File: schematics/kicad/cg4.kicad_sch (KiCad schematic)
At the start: 0 parts

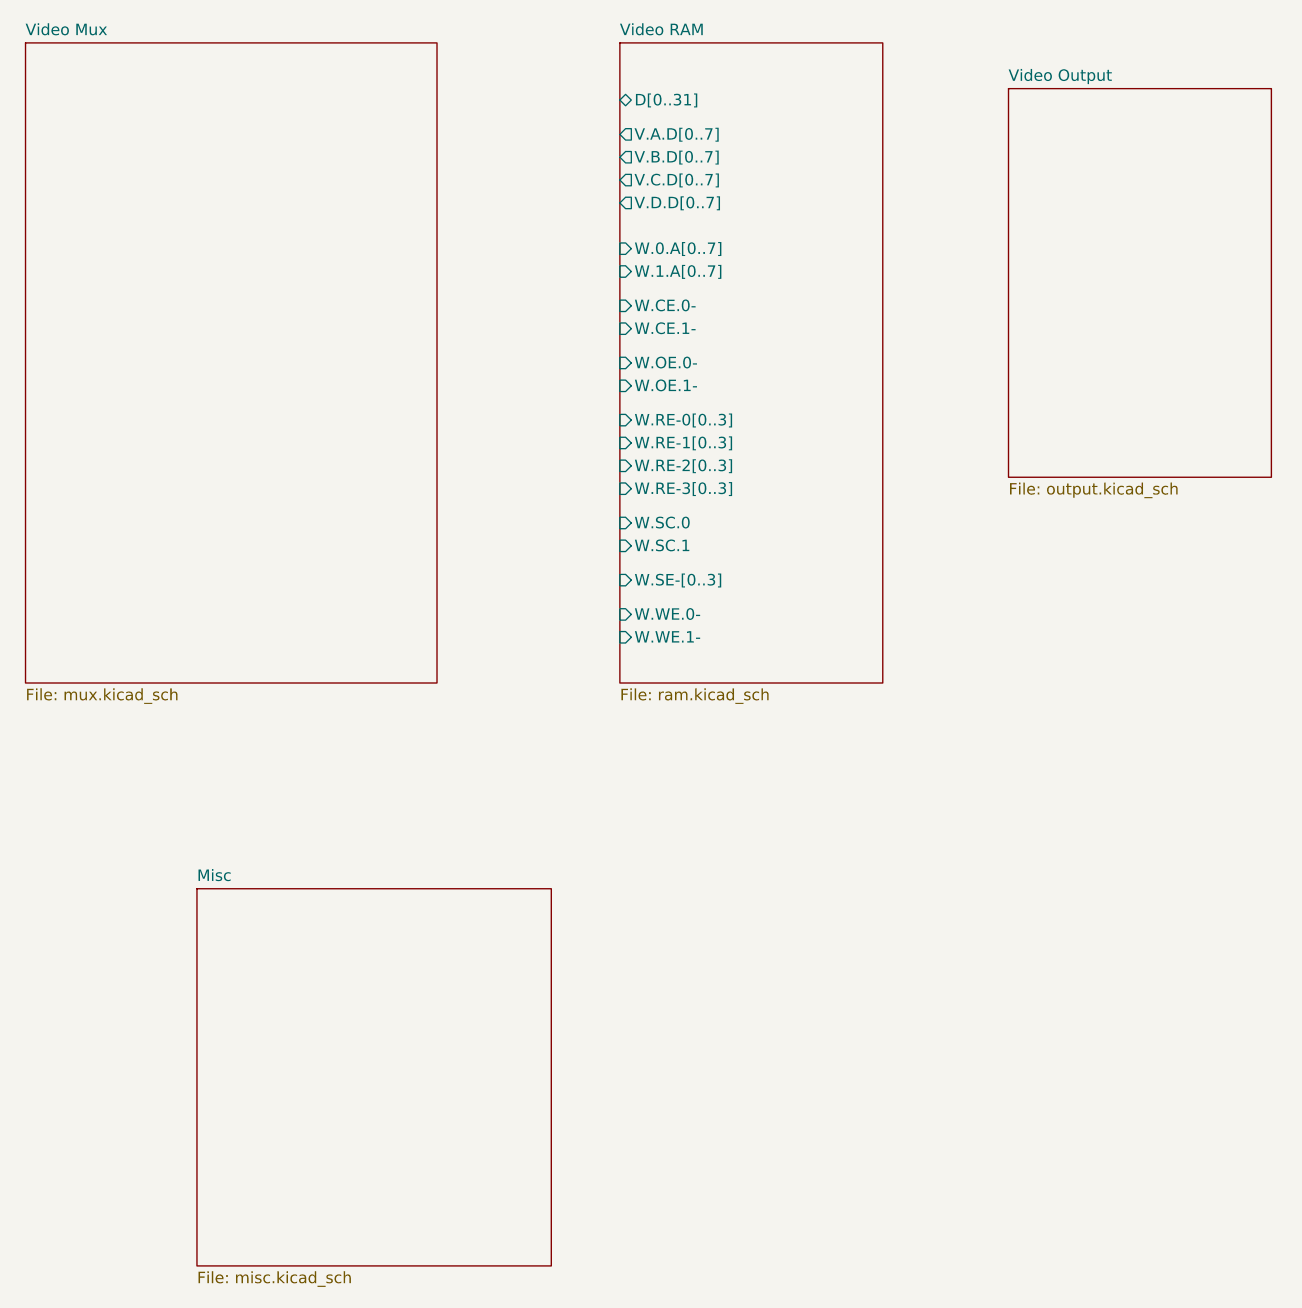
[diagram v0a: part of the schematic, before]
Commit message: Fill in more output section
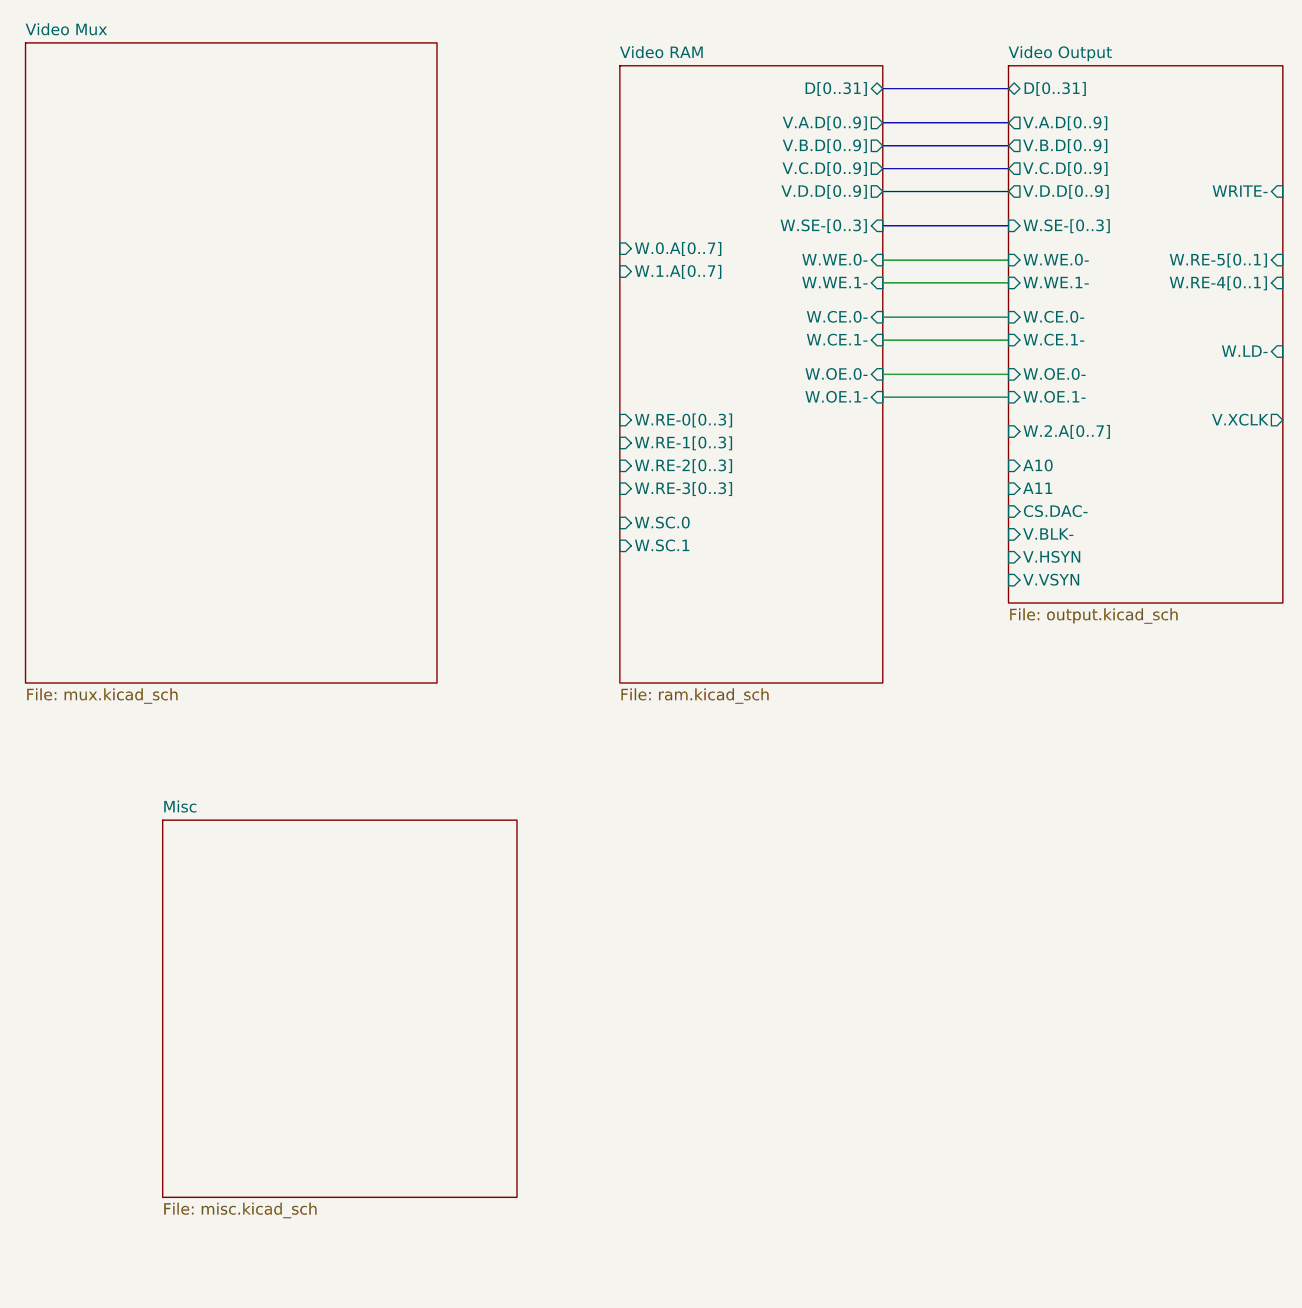
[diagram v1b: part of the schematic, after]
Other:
- sheet Video Output ports: added A10, A11, CS.DAC-, D[0..31], V.A.D[0..9], V.B.D[0..9], V.BLK-, V.C.D[0..9], V.D.D[0..9], V.HSYN, V.VSYN, V.XCLK, W.2.A[0..7], W.CE.0-, W.CE.1-, W.LD-, W.OE.0-, W.OE.1-, W.RE-4[0..1], W.RE-5[0..1], W.SE-[0..3], W.WE.0-, W.WE.1-, WRITE-; removed none
- sheet Video RAM ports: added V.A.D[0..9], V.B.D[0..9], V.C.D[0..9], V.D.D[0..9]; removed V.A.D[0..7], V.B.D[0..7], V.C.D[0..7], V.D.D[0..7]

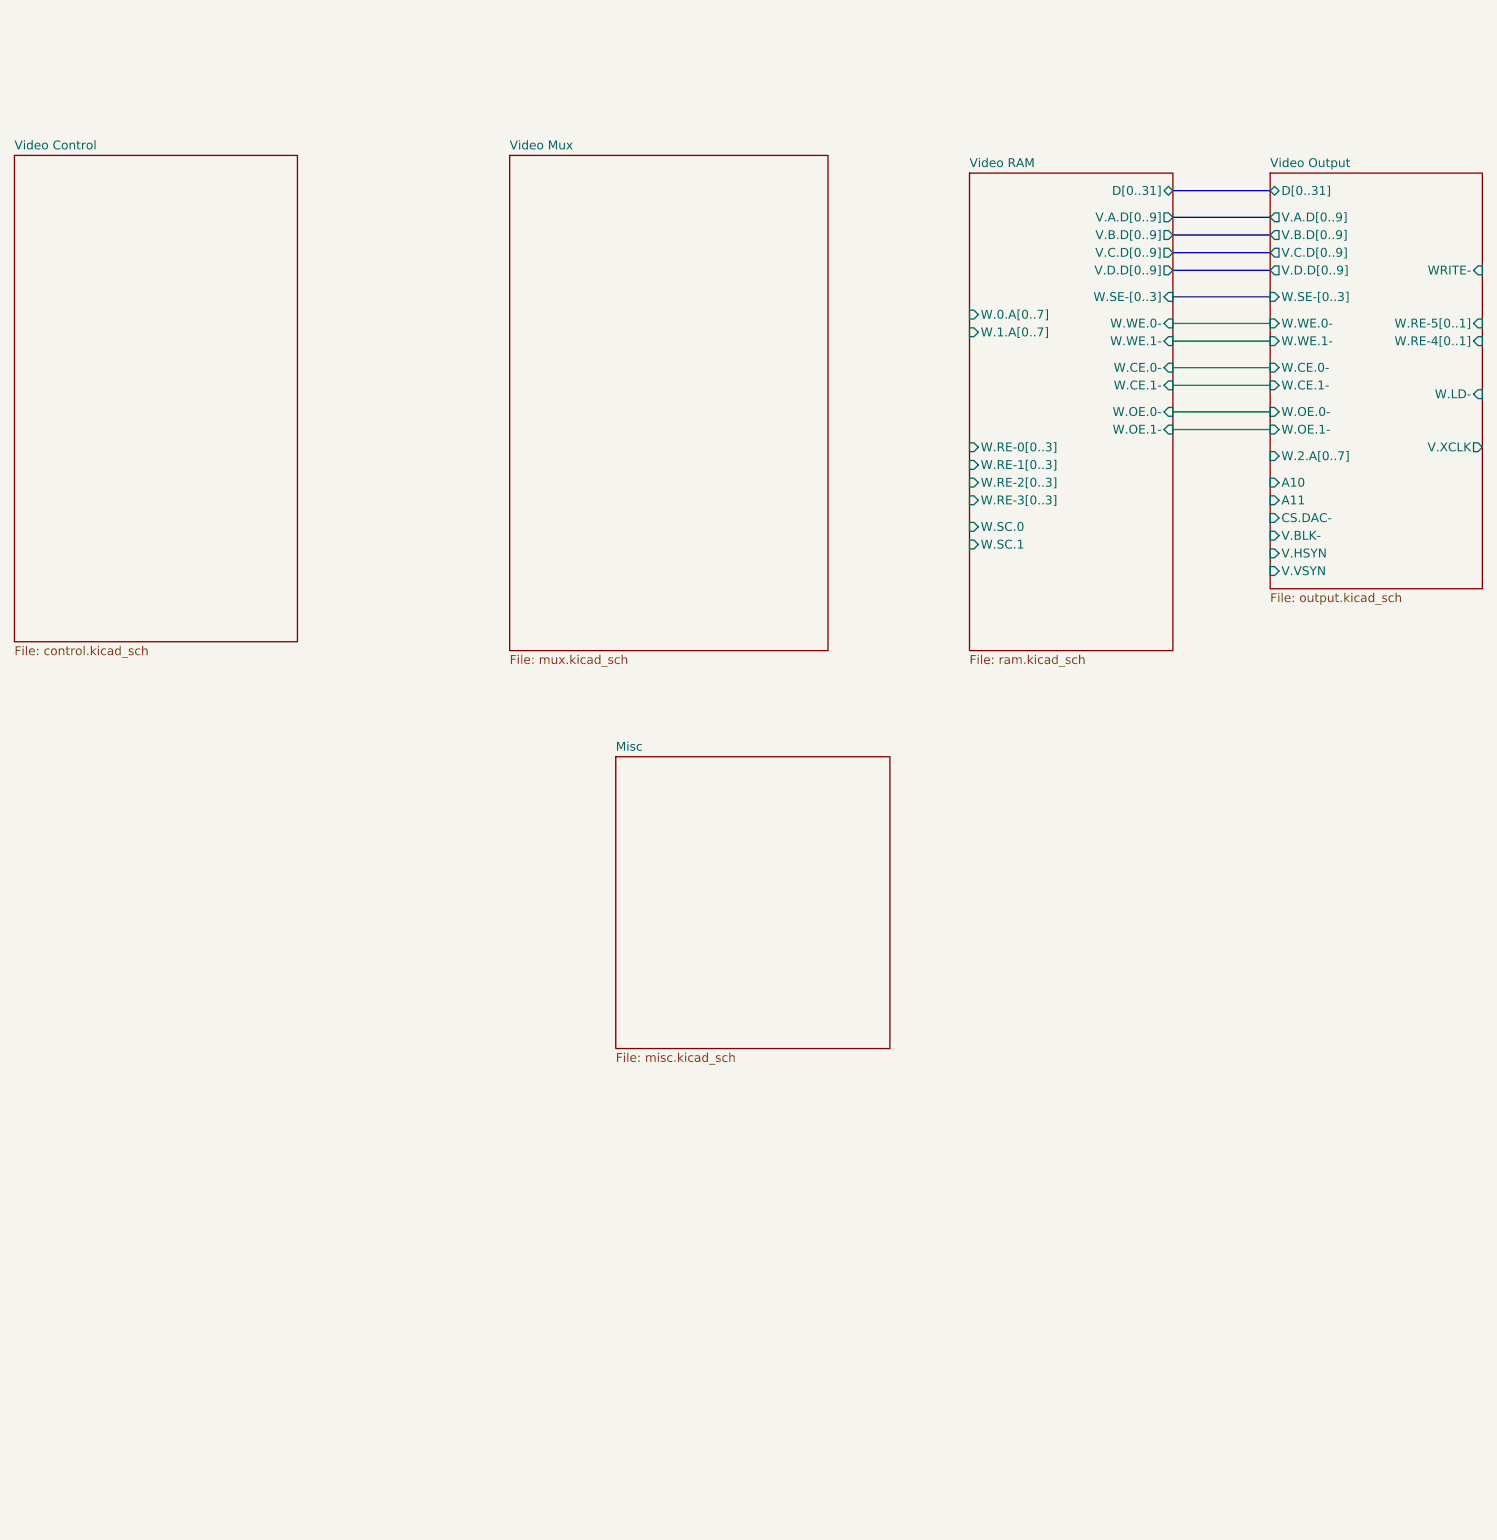
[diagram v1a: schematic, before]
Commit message: Populate misc page with P4 connector and caps Finish MUX, RAM and most of Output Lots of progress on Control Lay out root and connect most components
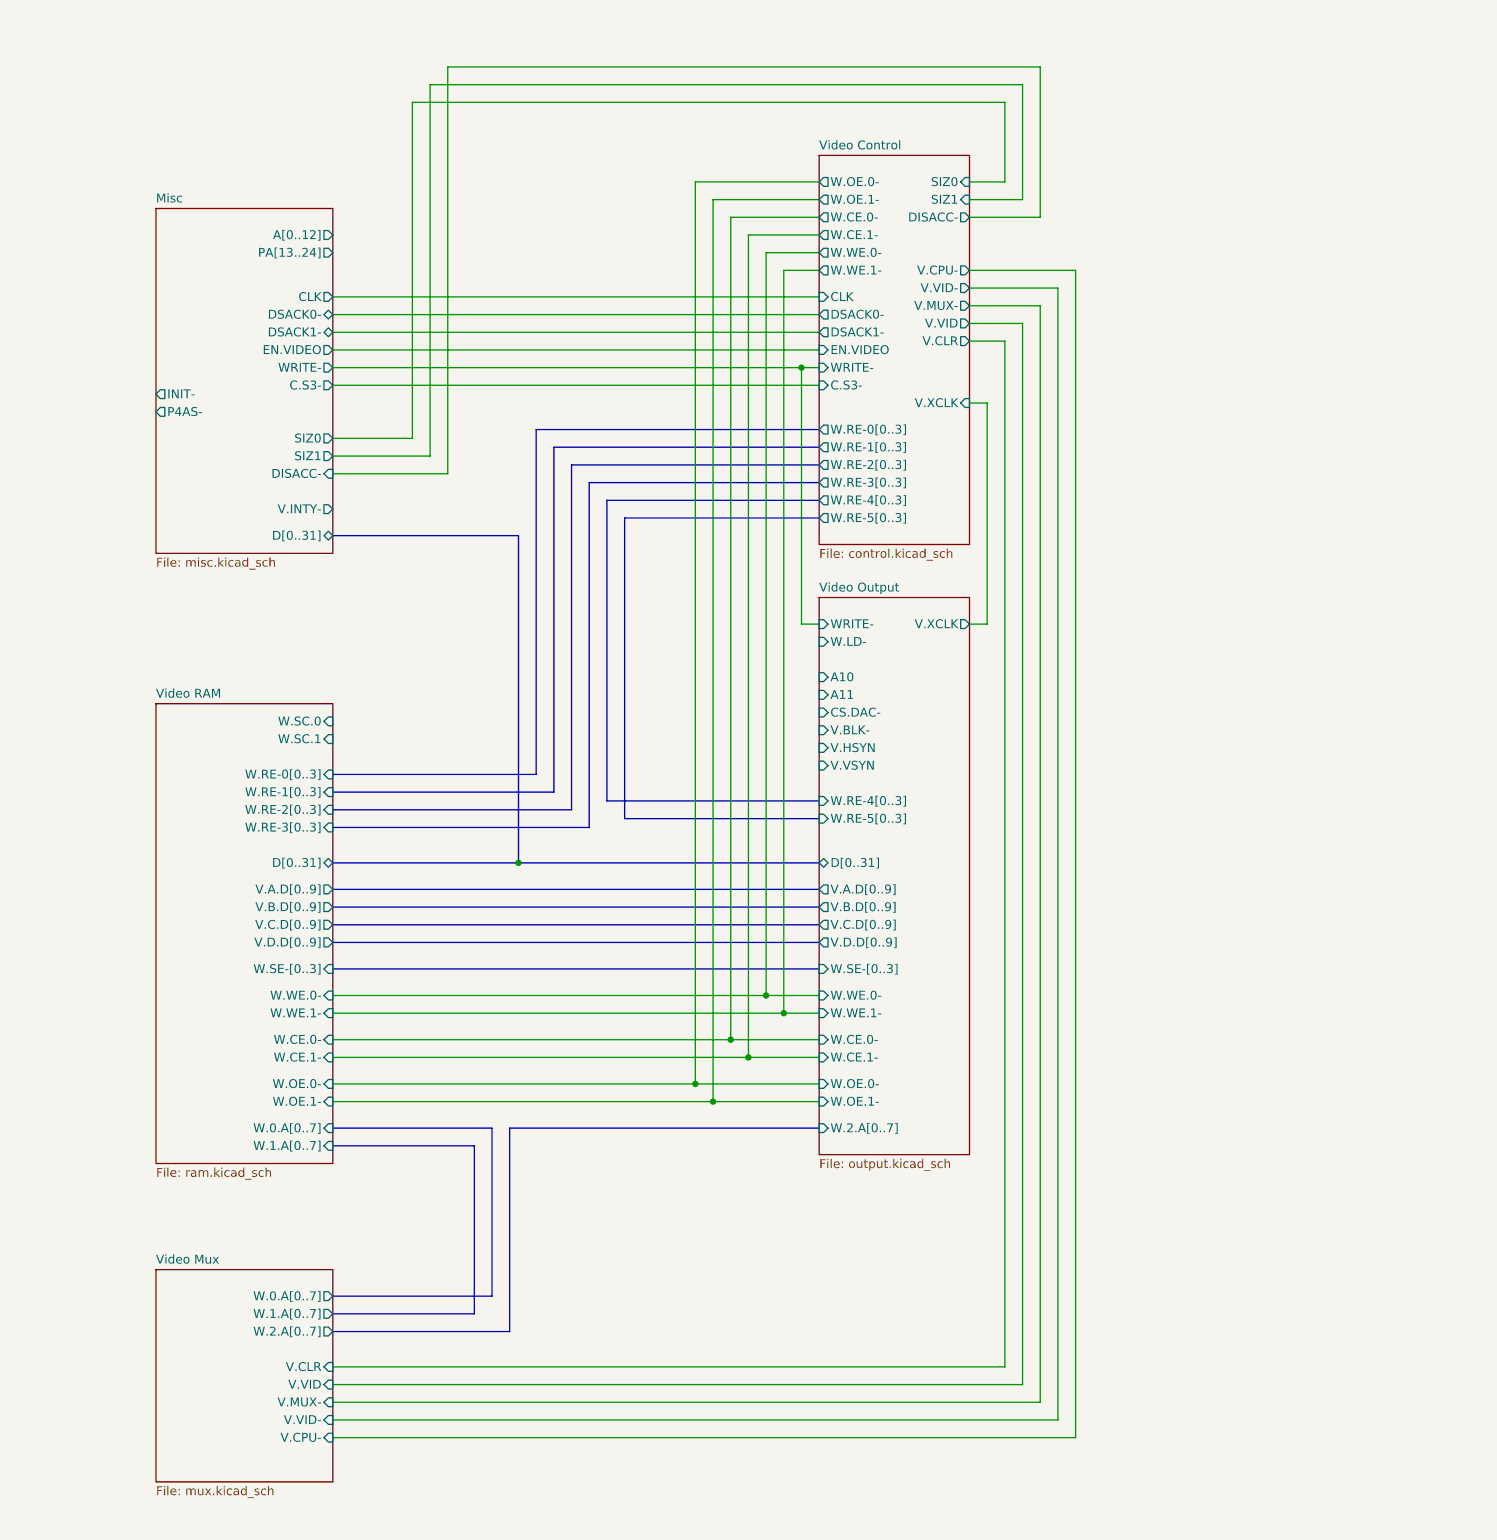
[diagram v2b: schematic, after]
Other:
- sheet Misc ports: added A[0..12], C.S3-, CLK, DISACC-, DSACK0-, DSACK1-, D[0..31], EN.VIDEO, INIT-, P4AS-, PA[13..24], SIZ0, SIZ1, V.INTY-, WRITE-; removed none
- sheet Video Control ports: added C.S3-, CLK, DISACC-, DSACK0-, DSACK1-, EN.VIDEO, SIZ0, SIZ1, V.CLR, V.CPU-, V.MUX-, V.VID, V.VID-, V.XCLK, W.CE.0-, W.CE.1-, W.OE.0-, W.OE.1-, W.RE-0[0..3], W.RE-1[0..3], W.RE-2[0..3], W.RE-3[0..3], W.RE-4[0..3], W.RE-5[0..3], W.WE.0-, W.WE.1-, WRITE-; removed none
- sheet Video Mux ports: added V.CLR, V.CPU-, V.MUX-, V.VID, V.VID-, W.0.A[0..7], W.1.A[0..7], W.2.A[0..7]; removed none
- sheet Video Output ports: added W.RE-4[0..3], W.RE-5[0..3]; removed W.RE-4[0..1], W.RE-5[0..1]

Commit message: Fill in most of control, wire up addresses, and more
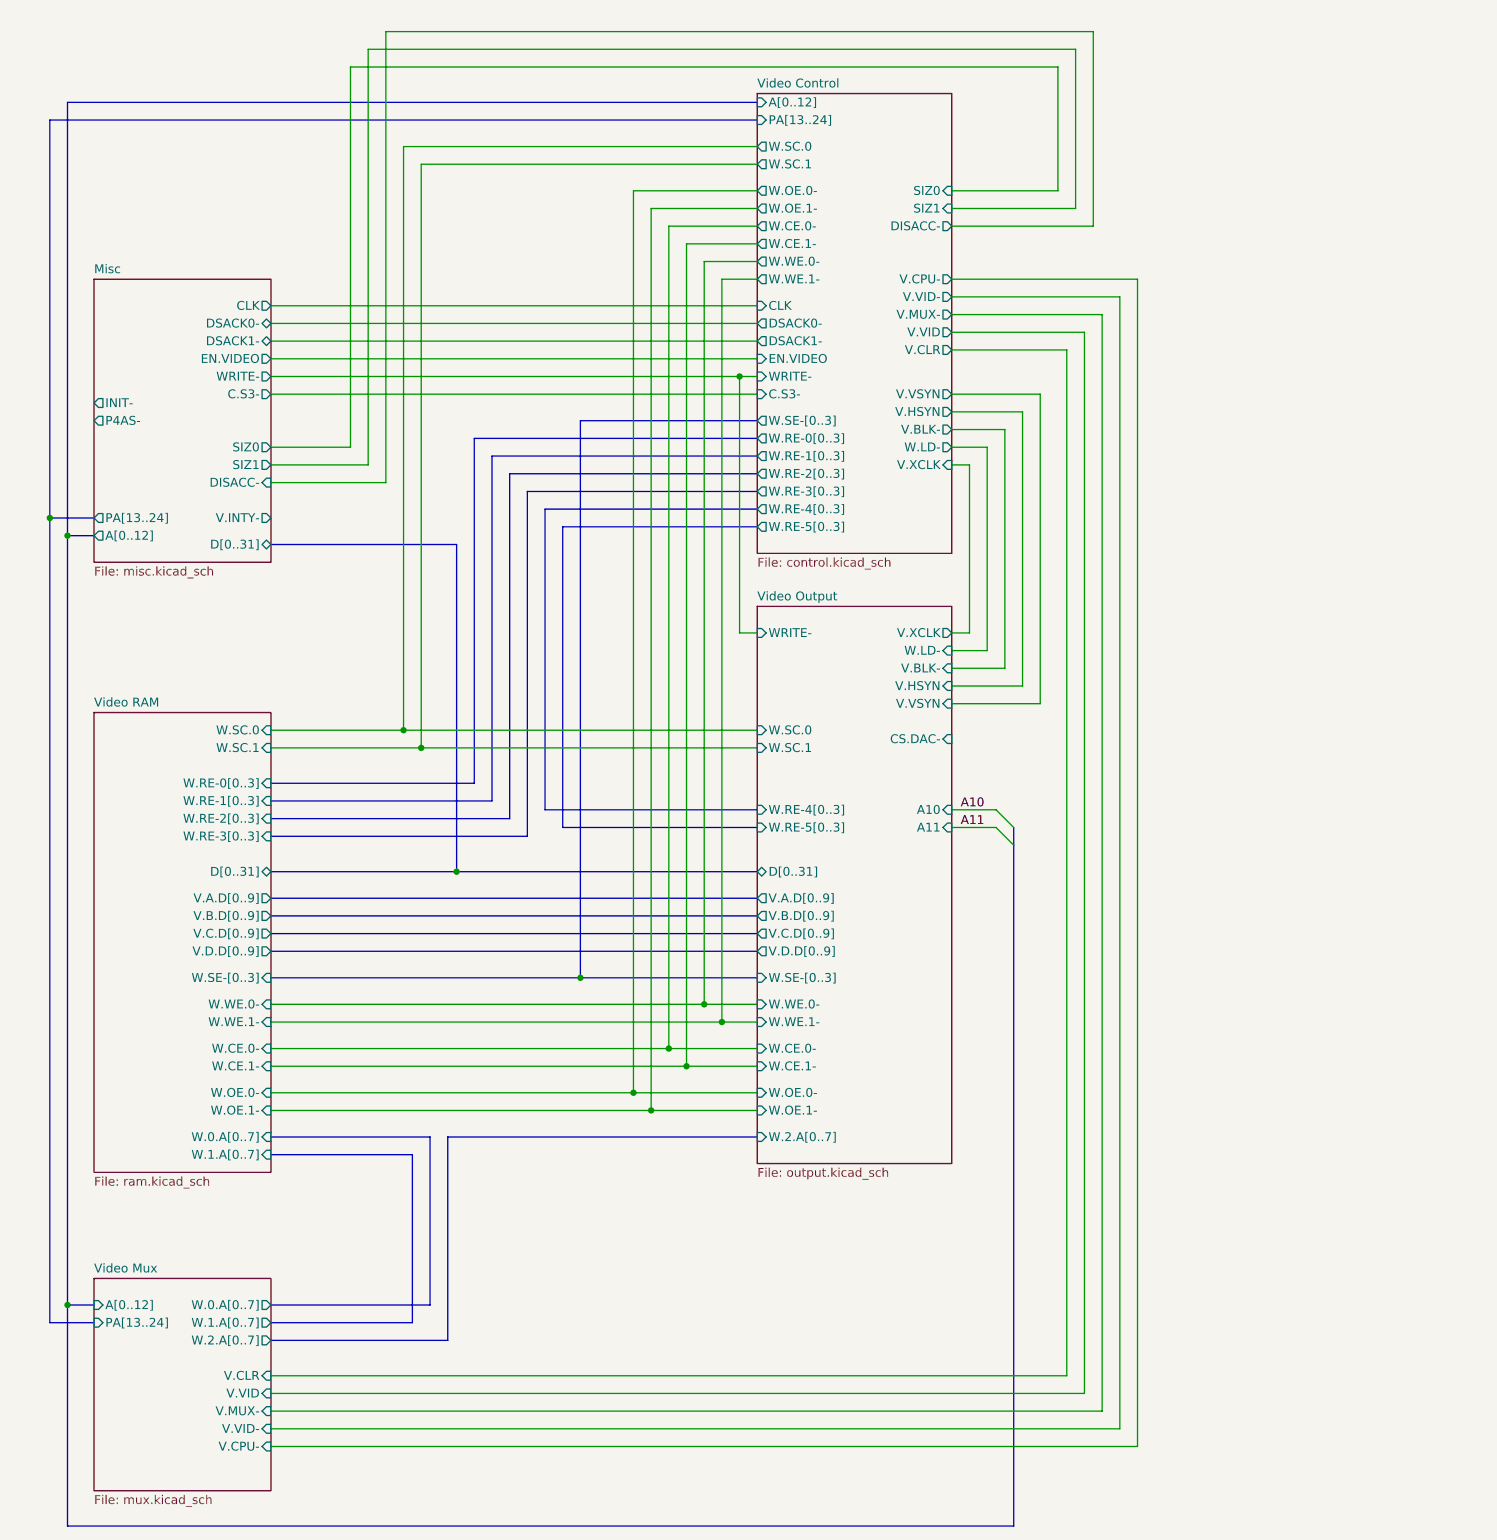
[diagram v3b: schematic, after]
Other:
- sheet Video Control ports: added A[0..12], PA[13..24], V.BLK-, V.HSYN, V.VSYN, W.LD-, W.SC.0, W.SC.1, W.SE-[0..3]; removed none
- sheet Video Mux ports: added A[0..12], PA[13..24]; removed none
- sheet Video Output ports: added W.SC.0, W.SC.1; removed none
